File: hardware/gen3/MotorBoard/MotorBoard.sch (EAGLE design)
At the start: 273 parts, among them M10O1 TEST_PT, M1O2 TEST_PT, M1O3 TEST_PT, M2O1 TEST_PT, M2O2 TEST_PT, M2O3 TEST_PT, M3O1 TEST_PT, M3O2 TEST_PT, M3O3 TEST_PT, M4O1 TEST_PT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

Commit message: fixed all DRC. vias in pads are ok, right?
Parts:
- renumbered M10O1 to M1O1
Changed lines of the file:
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@@
 <part name="M2O2" library="gen3" deviceset="TEST_PT" device=""/>
 <part name="M2O3" library="gen3" deviceset="TEST_PT" device=""/>
-<part name="M10O1" library="gen3" deviceset="TEST_PT" device=""/>
+<part name="M1O1" library="gen3" deviceset="TEST_PT" device=""/>
 <part name="M1O2" library="gen3" deviceset="TEST_PT" device=""/>
 <part name="M1O3" library="gen3" deviceset="TEST_PT" device=""/>
@@
 <instance part="M2O2" gate="G$1" x="657.86" y="304.8"/>
 <instance part="M2O3" gate="G$1" x="652.78" y="302.26"/>
-<instance part="M10O1" gate="G$1" x="401.32" y="307.34"/>
+<instance part="M1O1" gate="G$1" x="401.32" y="307.34"/>
 <instance part="M1O2" gate="G$1" x="396.24" y="304.8"/>
 <instance part="M1O3" gate="G$1" x="391.16" y="302.26"/>
@@
 <junction x="490.22" y="309.88"/>
 <wire x1="464.82" y1="309.88" x2="490.22" y2="309.88" width="0.1524" layer="91"/>
-<pinref part="M10O1" gate="G$1" pin="P$1"/>
+<pinref part="M1O1" gate="G$1" pin="P$1"/>
 <junction x="401.32" y="304.8"/>
 </segment>

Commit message: added logos. generated gerbers
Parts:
- added U$9: LOGO, gen3:LOGO
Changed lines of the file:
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@@
 <layer number="56" name="wert" color="7" fill="1" visible="no" active="no"/>
 <layer number="57" name="tCAD" color="7" fill="1" visible="no" active="no"/>
+<layer number="59" name="tCarbon" color="7" fill="1" visible="no" active="no"/>
+<layer number="60" name="bCarbon" color="7" fill="1" visible="no" active="no"/>
 <layer number="90" name="Modules" color="5" fill="1" visible="yes" active="yes"/>
 <layer number="91" name="Nets" color="2" fill="1" visible="yes" active="yes"/>
@@
 <layer number="127" name="_tValues" color="7" fill="1" visible="yes" active="yes"/>
 <layer number="128" name="_bValues" color="7" fill="1" visible="yes" active="yes"/>
+<layer number="129" name="Mask" color="7" fill="1" visible="yes" active="yes"/>
 <layer number="131" name="tAdjust" color="7" fill="1" visible="yes" active="yes"/>
 <layer number="132" name="bAdjust" color="7" fill="1" visible="yes" active="yes"/>
@@
 <layer number="251" name="SMDround" color="12" fill="11" visible="no" active="no"/>
 <layer number="254" name="cooling" color="7" fill="1" visible="yes" active="yes"/>
+<layer number="255" name="routoute" color="7" fill="1" visible="yes" active="yes"/>
 </layers>
 <schematic xreflabel="%F%N/%S.%C%R" xrefpart="/%S.%C%R">
@@
 <part name="C45" library="SparkFun-Capacitors" deviceset="CAP" device="0805" value="1uF"/>
 <part name="C46" library="SparkFun-Capacitors" deviceset="CAP" device="0805" value=".01uF"/>
+<part name="U$9" library="gen3" deviceset="LOGO" device=""/>
 </parts>
 <sheets>
@@
 <instance part="C45" gate="G$1" x="101.6" y="167.64" rot="R90"/>
 <instance part="C46" gate="G$1" x="101.6" y="157.48" rot="R90"/>
+<instance part="U$9" gate="G$1" x="35.56" y="91.44"/>
 </instances>
 <busses>

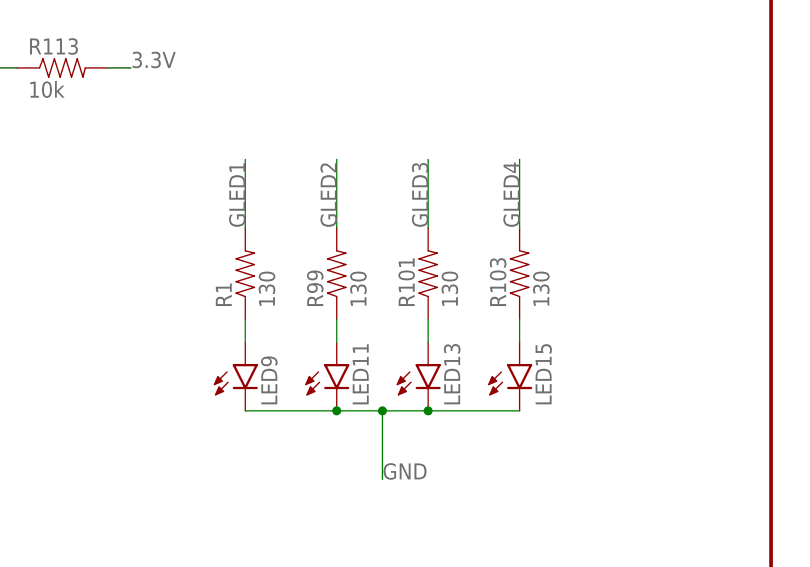
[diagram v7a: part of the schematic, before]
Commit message: resistor values for LEDs
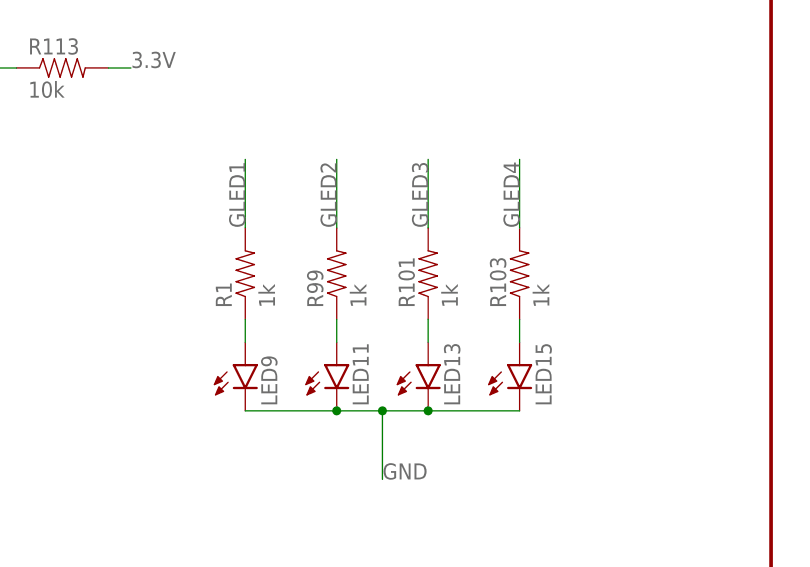
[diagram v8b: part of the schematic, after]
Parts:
- R1, R101, R103, R99: value 130 -> 1k
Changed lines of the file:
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@@
 <part name="R97" library="SparkFun-Passives" deviceset="RESISTOR" device="0805-RES" value="10k"/>
 <part name="U2" library="Atmel_By_element14_Batch_1-00" deviceset="ATMEGA165PV-8AU" device=""/>
-<part name="R1" library="SparkFun-Passives" deviceset="RESISTOR" device="0805-RES" value="130"/>
-<part name="R99" library="SparkFun-Passives" deviceset="RESISTOR" device="0805-RES" value="130"/>
-<part name="R101" library="SparkFun-Passives" deviceset="RESISTOR" device="0805-RES" value="130"/>
-<part name="R103" library="SparkFun-Passives" deviceset="RESISTOR" device="0805-RES" value="130"/>
+<part name="R1" library="SparkFun-Passives" deviceset="RESISTOR" device="0805-RES" value="1k"/>
+<part name="R99" library="SparkFun-Passives" deviceset="RESISTOR" device="0805-RES" value="1k"/>
+<part name="R101" library="SparkFun-Passives" deviceset="RESISTOR" device="0805-RES" value="1k"/>
+<part name="R103" library="SparkFun-Passives" deviceset="RESISTOR" device="0805-RES" value="1k"/>
 <part name="LED9" library="SparkFun-LED" deviceset="LED" device="1206"/>
 <part name="LED11" library="SparkFun-LED" deviceset="LED" device="1206"/>
